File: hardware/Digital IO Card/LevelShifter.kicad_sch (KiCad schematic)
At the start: 8 parts, among them U36 SN74ACT17PWR, U38 SN74AHC1G125

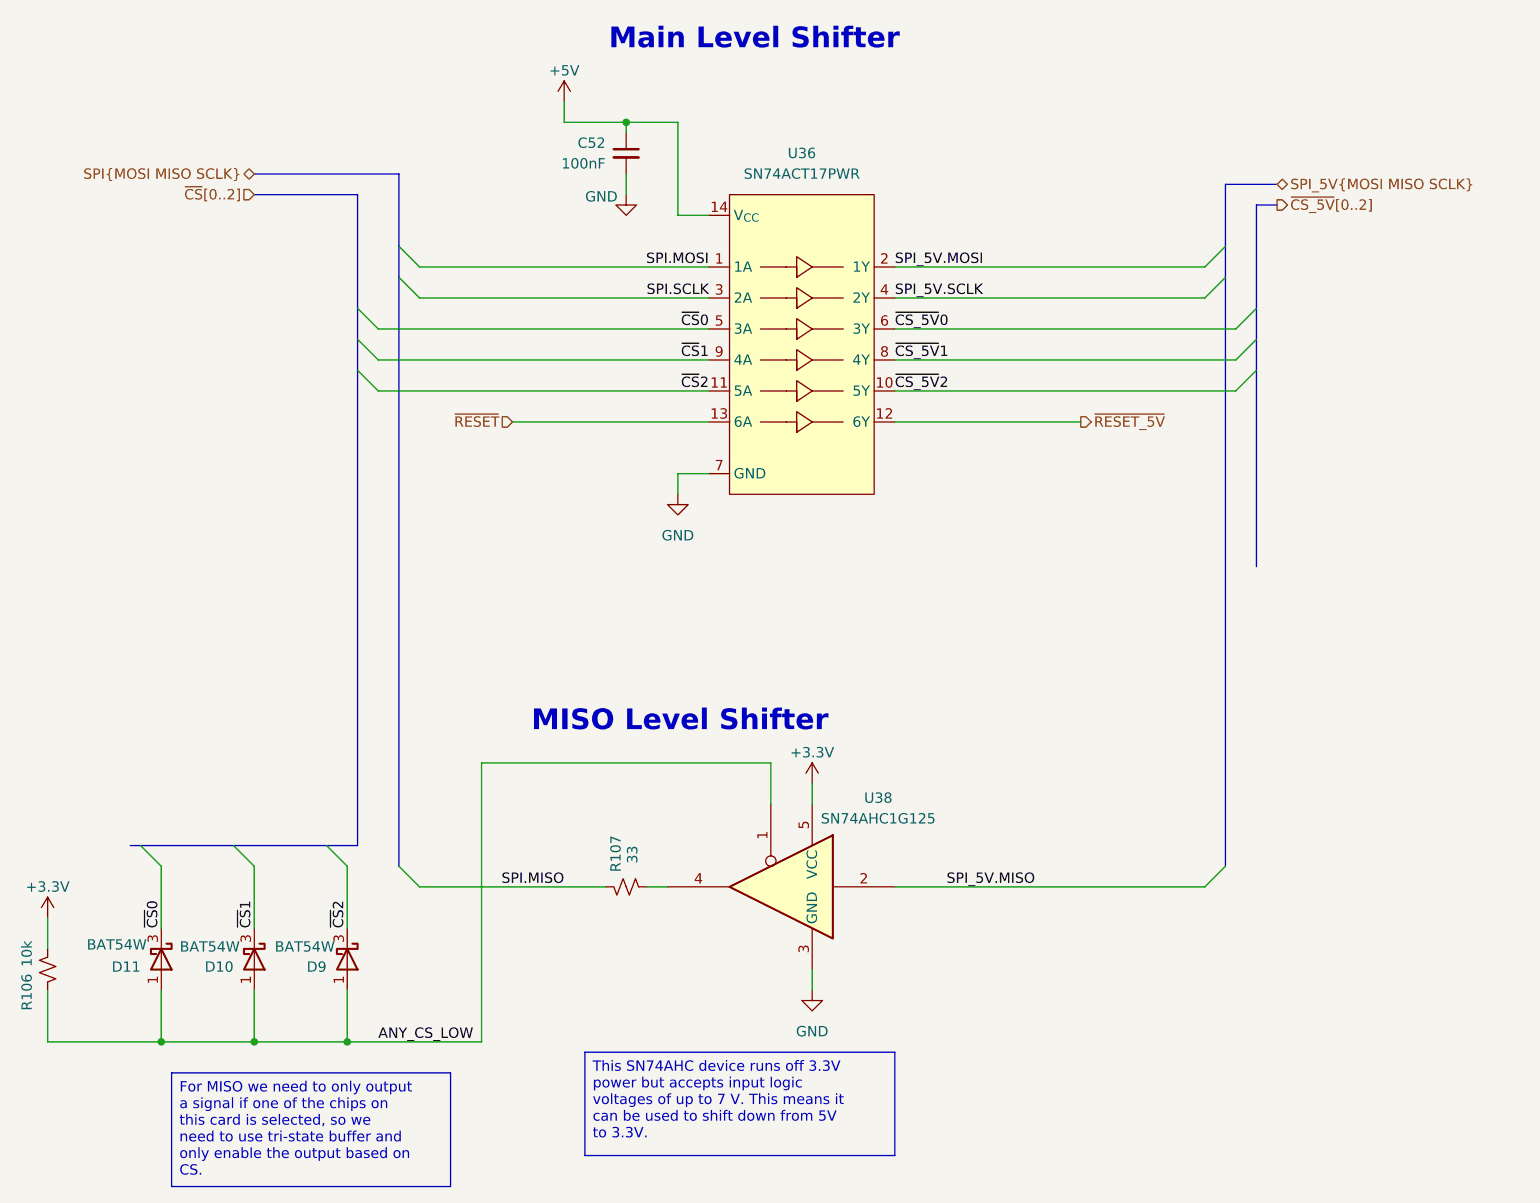
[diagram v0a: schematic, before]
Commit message: Start redoing DIO card
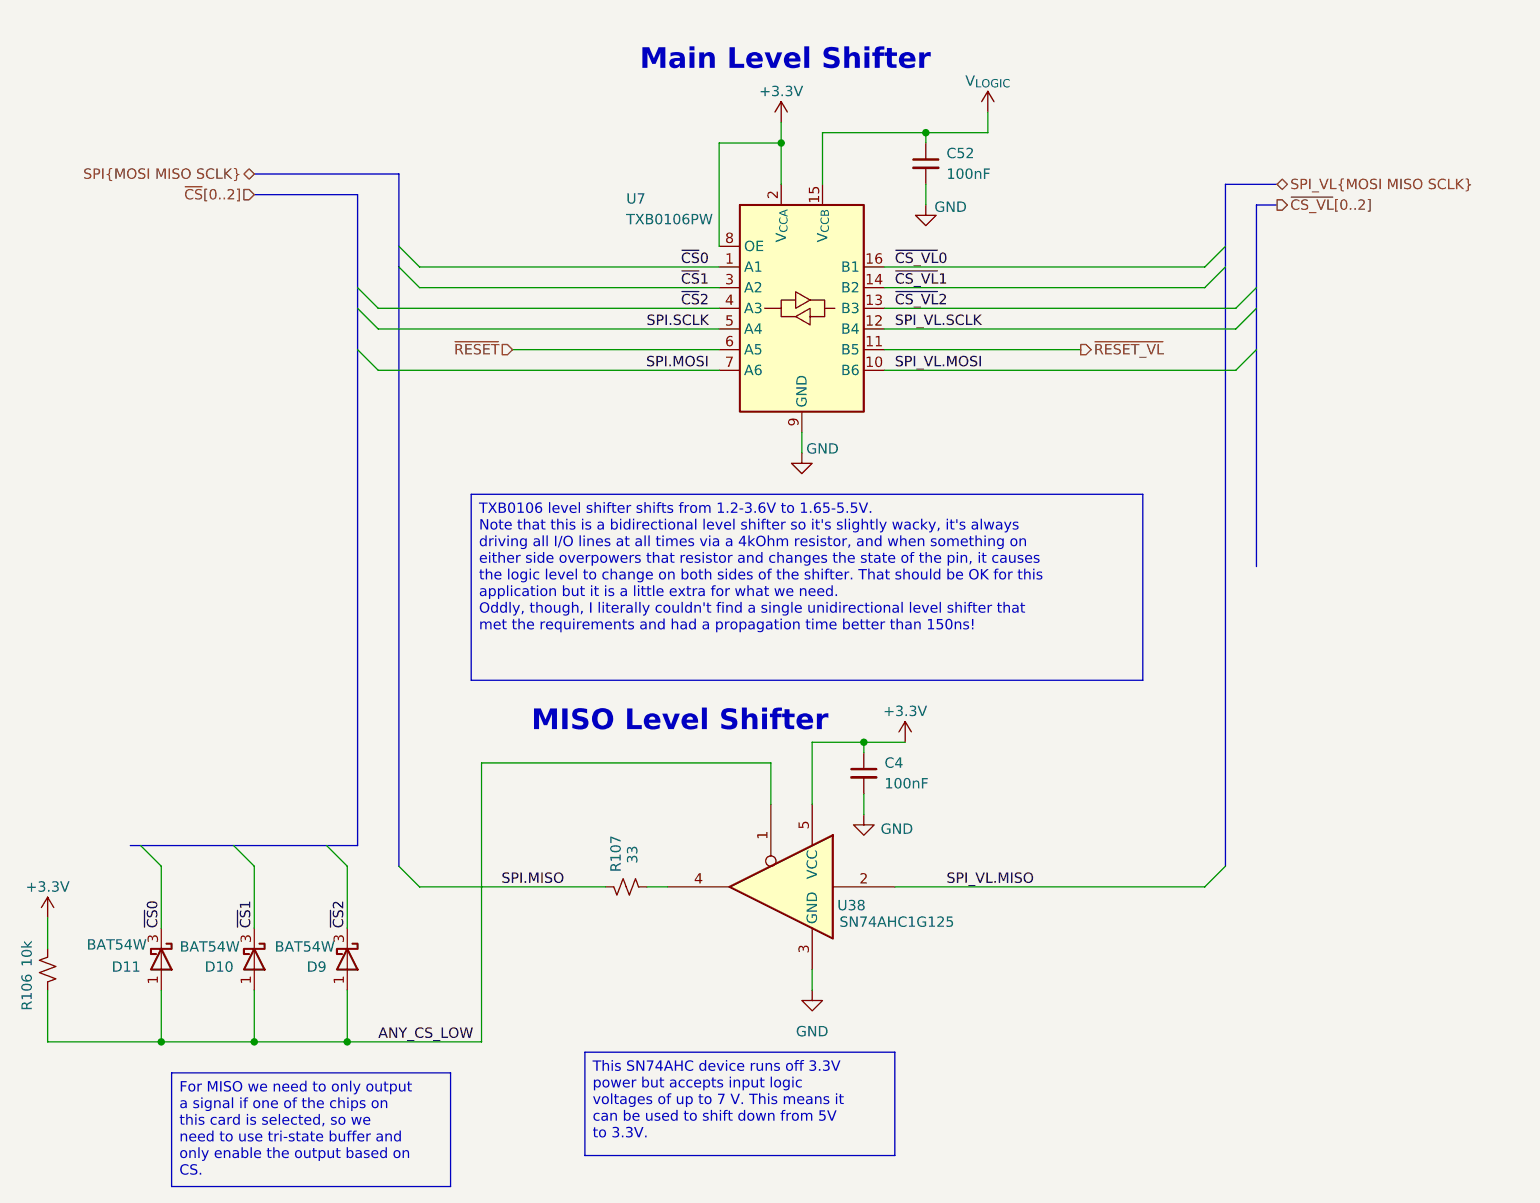
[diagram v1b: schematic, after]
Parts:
- removed U36: SN74ACT17PWR, Package_SO:TSSOP-14_4.4x5mm_P0.65mm, symbol Project Library:SN74ACT17
- added C4: 100nF, Capacitor_SMD:C_0603_1608Metric, symbol Device:C_Small
- added U7: TXB0106PW, Package_SO:TSSOP-16_4.4x5mm_P0.65mm, symbol Logic_LevelTranslator:TXB0106PW
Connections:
- net +3.3V: now also C4.1, U7.2 (V_{CCA}), U7.8 (OE)
- net GND: now also C4.2, U7.9 (GND)
- net SPI.MOSI: now also U7.7 (A6)
- net SPI.SCLK: now also U7.5 (A4)
- net ~{CS}0: now also U7.1 (A1)
- net ~{CS}1: now also U7.3 (A2)
- net ~{CS}2: now also U7.4 (A3)
- net ~{RESET}: now also U7.6 (A5)
- net +5V renamed V_{LOGIC}
- net V_{LOGIC}: now also U7.15 (V_{CCB})
- net SPI_5V.MISO renamed SPI_VL.MISO
- new net SPI_VL.MOSI: U7.10 (B6)
- new net SPI_VL.SCLK: U7.12 (B4)
- new net ~{CS_VL}0: U7.16 (B1)
- new net ~{CS_VL}1: U7.14 (B2)
- new net ~{CS_VL}2: U7.13 (B3)
- new net ~{RESET_VL}: U7.11 (B5)
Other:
- moved on the sheet: C52
